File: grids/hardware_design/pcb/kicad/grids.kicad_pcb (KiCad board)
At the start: 2 copper layers, 78.1 x 102.9 mm, 108 parts, among them IC1 ATMEGA328P-AU, IC2 LM4040 5.0V, IC3 MCP6002, IC4 MCP6002, IC5 MCP6002, IC6 74HC595D, IC7 LM1117-5.0, J1 PJ301WQP, J10 PJ301WQP, J11 PJ301WQP, J12 PJ301WQP, J13 PJ301WQP, J14 PJ301WQP, J16 M05X2PTH, J2 PJ301WQP, J3 PJ301WQP, J4 PJ301WQP, J5 PJ301WQP, J6 PJ301WQP, J7 PJ301WQP, J8 PJ301WQP, J9 PJ301WQP, Q1 20MHz, Q2 MMBT3904, Q3 MMBT3904, SW1 LP4OA1PBCT

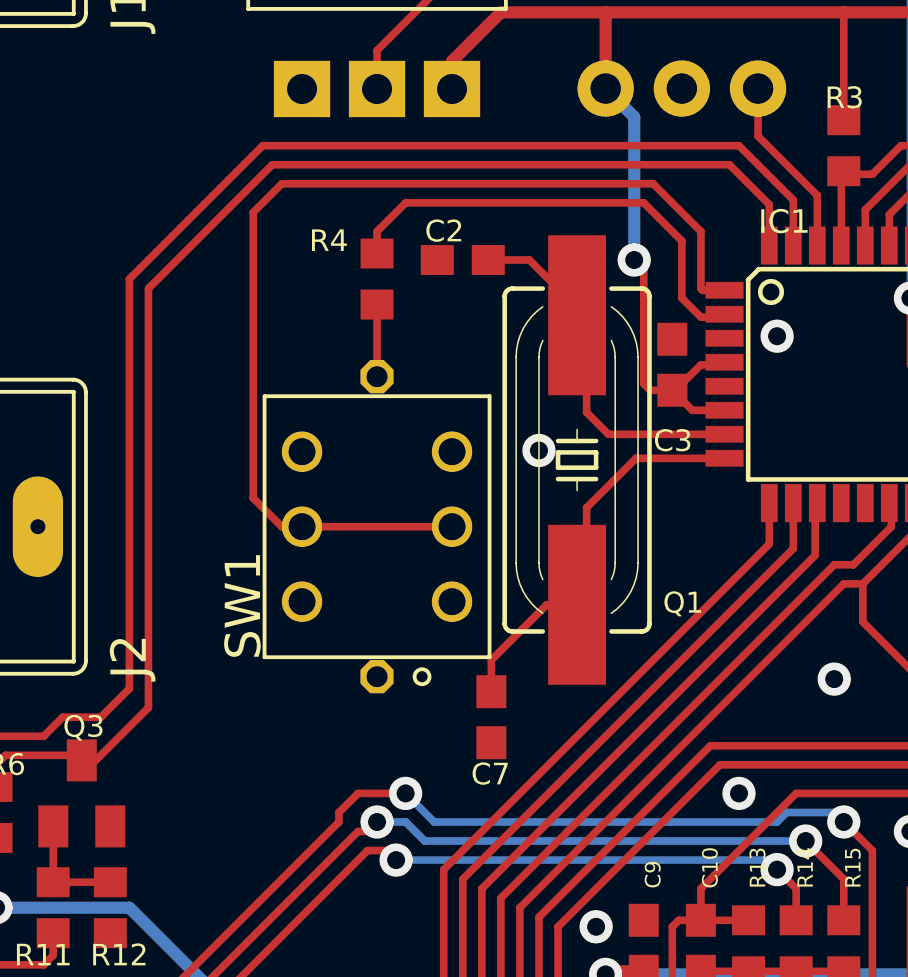
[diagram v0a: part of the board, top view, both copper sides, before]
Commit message: change LED/SW and crystal
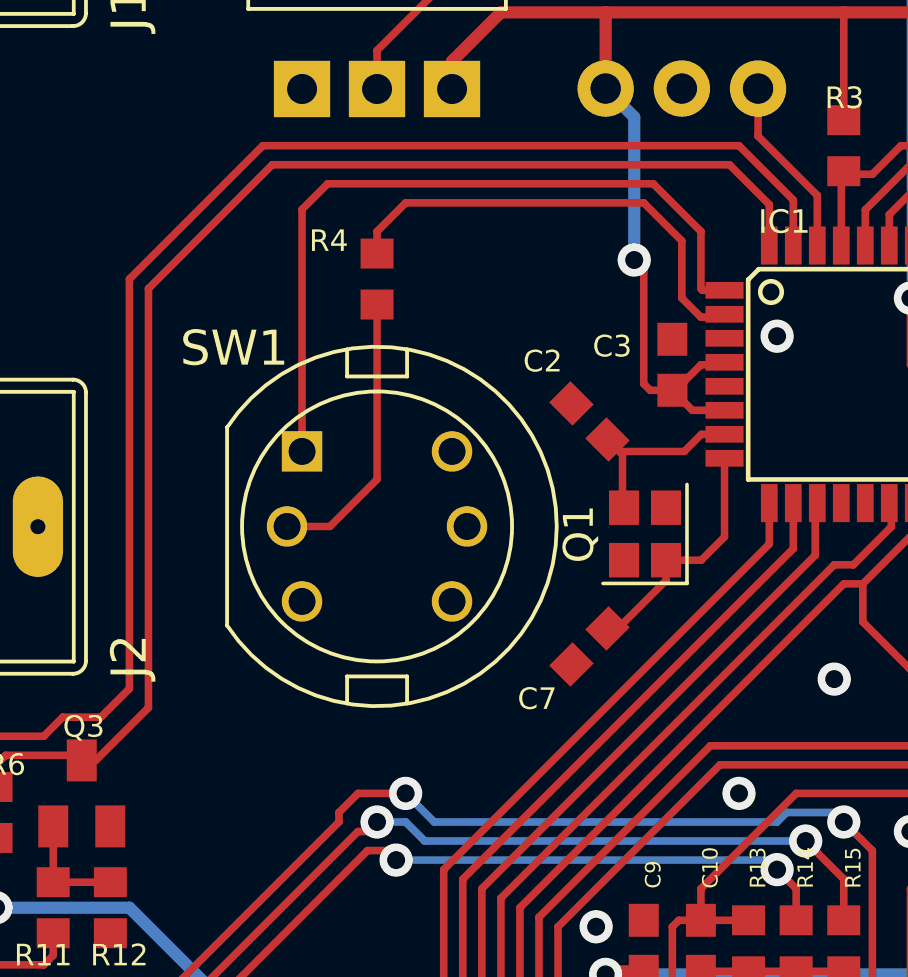
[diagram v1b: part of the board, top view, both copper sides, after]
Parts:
- removed U$1: , grids:EURORACK_TEMPLATE
- removed U$2: , grids:ROHS_BIG
- IC6: value 74HC595D -> 74595D
- J15: value (none) -> AVR_SPI_PRG_6PTH
- JP1, JP2: value (none) -> M03PTH
- L1: value (none) -> WE-CBF_0603
- LED2, LED3, LED4: value (none) -> LED3MM
- Q1: footprint grids:HC49UP -> Crystal:Crystal_SMD_2520-4Pin_2.5x2.0mm
- SW1: value LP4OA1PBCT -> SW_MEC_5G_2LED; footprint grids:LP4OA1PBCT -> Supercell 1.3:C&K_D6R
- moved C2 6.84 mm to (139.4, 78.0), turned to -45 degrees
- moved C7 4.03 mm to (139.4, 85.5), turned to 45 degrees
- moved Q1 3.35 mm to (141.2, 81.8)
- turned SW1 to 0 degrees
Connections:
- net AREF renamed /AREF
- net CH1_CV renamed /CH1_CV
- net CH2_CV renamed /CH2_CV
- net CH3_CV renamed /CH3_CV
- net CLOCK_OUT renamed Net-(IC6-Pad6)
- net GATE1_IN renamed Net-(J1-PadTIP)
- net GATE2_IN renamed Net-(J2-PadTIP)
- net GATE2_LED renamed Net-(LED4-PadA)
- net GATE3_LED renamed Net-(LED3-PadA)
- net GATE4_LED renamed Net-(LED2-PadA)
- net IN_CLOCK renamed /IN_CLOCK
- net IN_MIDI renamed /IN_MIDI
- net IN_RESET renamed /IN_RESET
- net LED_CH1 renamed /LED_CH1
- net LED_CH2 renamed /LED_CH2
- net LED_CH3 renamed /LED_CH3
- net LED_CLOCK renamed /LED_CLOCK
- net MISO renamed /MISO
- net MOSI renamed /MOSI
- net RANDOM_GATE renamed Net-(IC6-Pad7)
- net REF_-5 renamed /REF_-5
- net RESET renamed /RESET
- net RND_CV renamed /RND_CV
- net SCK renamed /SCK
- net SS renamed /SS
- net TEMPO renamed /TEMPO
- net X_CV renamed /X_CV
- net Y_CV renamed /Y_CV
- C2 pad 2: N$83 -> Net-(C2-Pad2)
- IC1 pad 1: SW_RESET -> /SW_RESET
- IC1 pad 12: (no net) -> unconnected-(IC1-Pad12)
- IC1 pad 13: (no net) -> unconnected-(IC1-Pad13)
- IC1 pad 22: (no net) -> unconnected-(IC1-Pad22)
- IC1 pad 7: N$83 -> Net-(C2-Pad2)
- IC6 pad 9: (no net) -> unconnected-(IC6-Pad9)
- J1 pad SW: (no net) -> unconnected-(J1-PadSW)
- J10 pad SW: (no net) -> unconnected-(J10-PadSW)
- J11 pad SW: (no net) -> unconnected-(J11-PadSW)
- J12 pad SW: (no net) -> unconnected-(J12-PadSW)
- J13 pad SW: (no net) -> unconnected-(J13-PadSW)
- J14 pad SW: (no net) -> unconnected-(J14-PadSW)
- J16 pad 2: (no net) -> unconnected-(J16-Pad2)
- J2 pad SW: (no net) -> unconnected-(J2-PadSW)
- J3 pad SW: (no net) -> unconnected-(J3-PadSW)
- J4 pad SW: (no net) -> unconnected-(J4-PadSW)
- J5 pad SW: (no net) -> unconnected-(J5-PadSW)
- J6 pad SW: (no net) -> unconnected-(J6-PadSW)
- J7 pad SW: (no net) -> unconnected-(J7-PadSW)
- J8 pad SW: (no net) -> unconnected-(J8-PadSW)
- J9 pad SW: (no net) -> unconnected-(J9-PadSW)
- Q1 pad 2: N$83 -> unconnected-(Q1-Pad2)
- R4 pad 2: GATE1_LED -> Net-(SW1-Pad2)
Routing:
- net SW_RESET: track 35.2 -> 0.00 mm
- net /SW_RESET: track 0.00 -> 25.1 mm
- net N$83: track 12.1 -> 0.00 mm
- net Net-(SW1-Pad2): track 0.00 -> 9.48 mm
- net Net-(C2-Pad2): track 0.00 -> 6.80 mm
- net Net-(C7-Pad2): track 13.3 -> 8.18 mm
- net GATE1_LED: track 2.41 -> 0.00 mm
- net GND: vias 65 -> 64

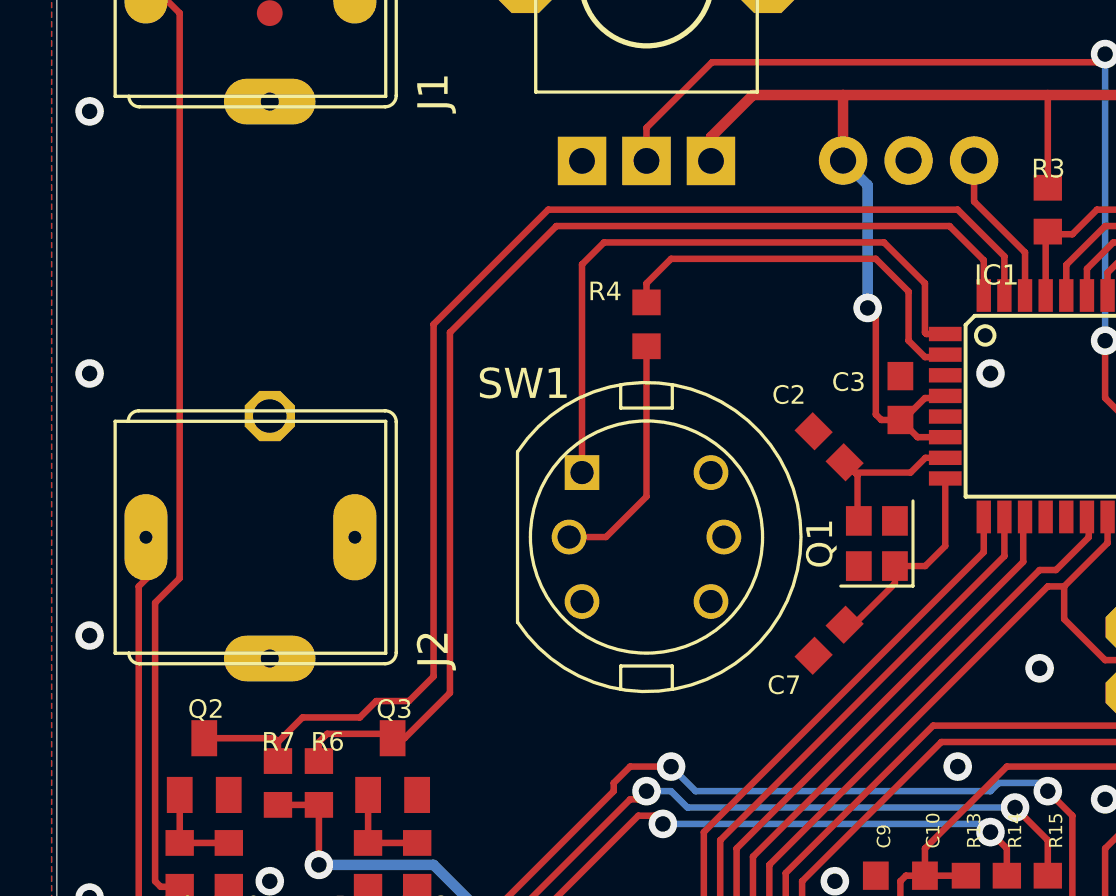
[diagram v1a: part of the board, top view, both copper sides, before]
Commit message: add horizontal smd programming header (traces not drawn yet)
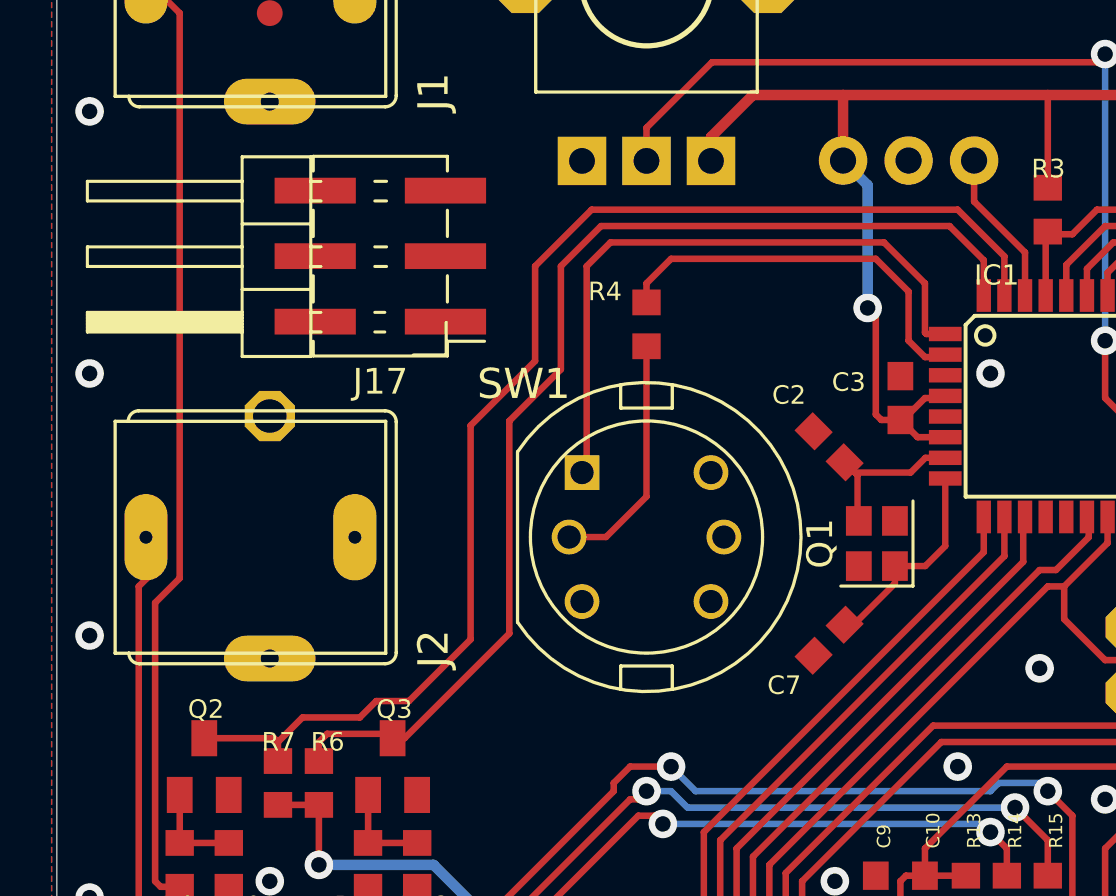
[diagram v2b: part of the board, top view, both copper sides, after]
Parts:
- added J17: AVR_SPI_PRG_6PTH, Connector_PinHeader_2.54mm:PinHeader_2x03_P2.54mm_Horizontal_SMD, F.Cu at (122.0, 70.6)
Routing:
- net /IN_RESET: track 45.0 -> 44.0 mm
- net /IN_CLOCK: track 50.6 -> 49.6 mm

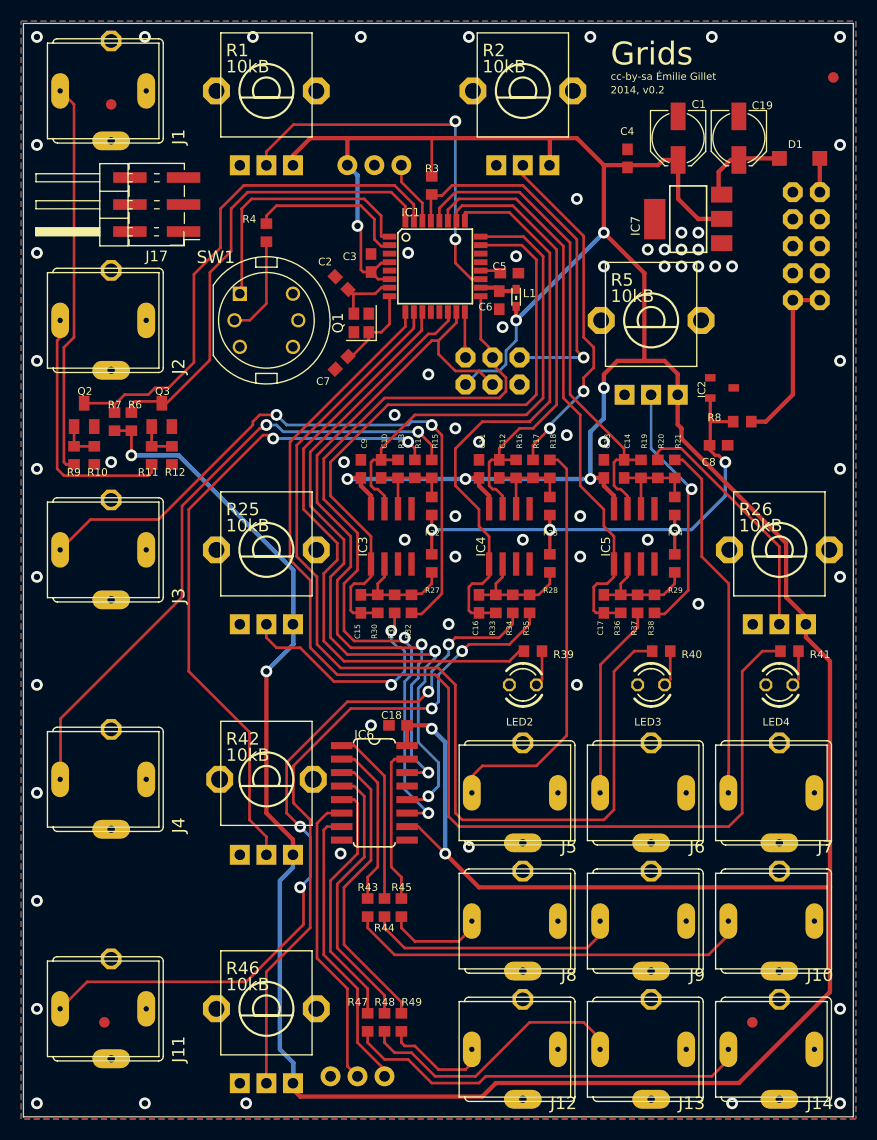
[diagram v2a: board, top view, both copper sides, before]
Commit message: changed jacks
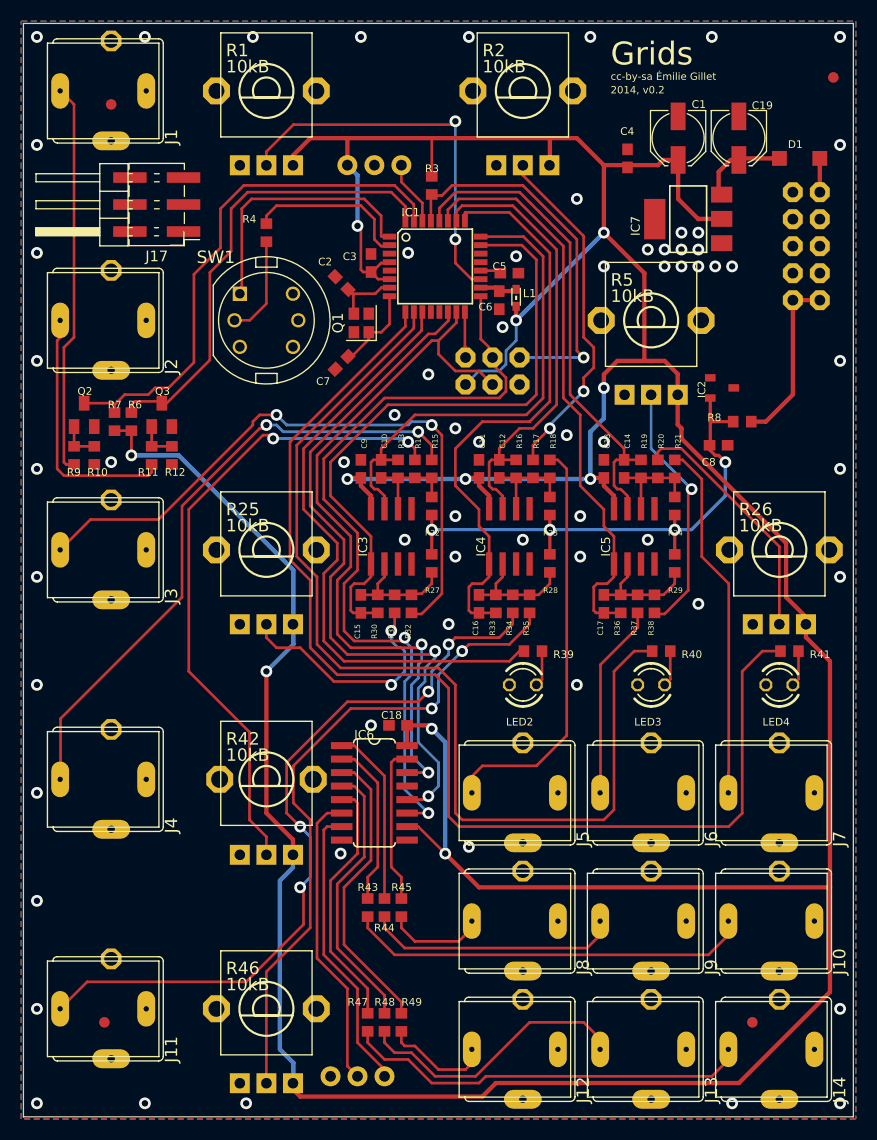
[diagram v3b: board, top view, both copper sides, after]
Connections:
- J1 pad GND2: GND -> (no net)
- J10 pad GND2: GND -> (no net)
- J11 pad GND2: GND -> (no net)
- J12 pad GND2: GND -> (no net)
- J13 pad GND2: GND -> (no net)
- J14 pad GND2: GND -> (no net)
- J2 pad GND2: GND -> (no net)
- J3 pad GND2: GND -> (no net)
- J4 pad GND2: GND -> (no net)
- J5 pad GND2: GND -> (no net)
- J6 pad GND2: GND -> (no net)
- J7 pad GND2: GND -> (no net)
- J8 pad GND2: GND -> (no net)
- J9 pad GND2: GND -> (no net)

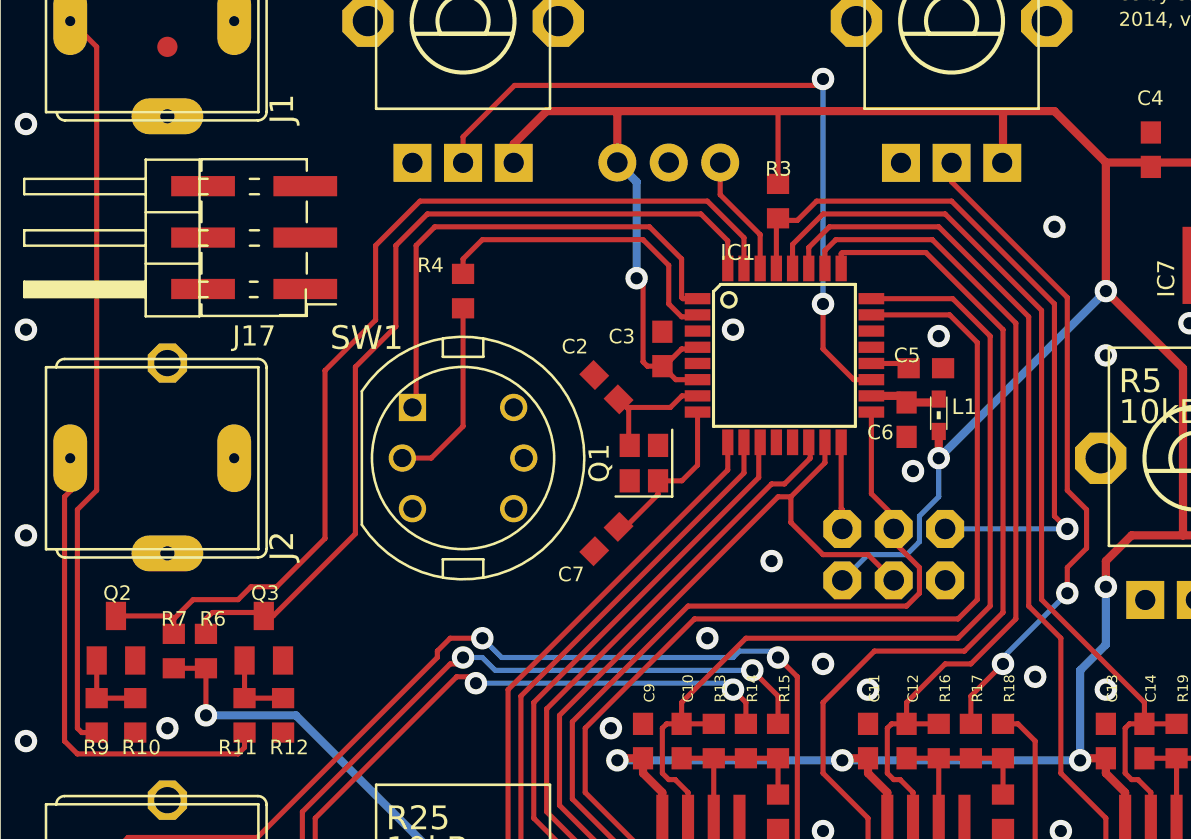
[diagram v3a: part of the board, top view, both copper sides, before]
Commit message: draw pcb traces for new header
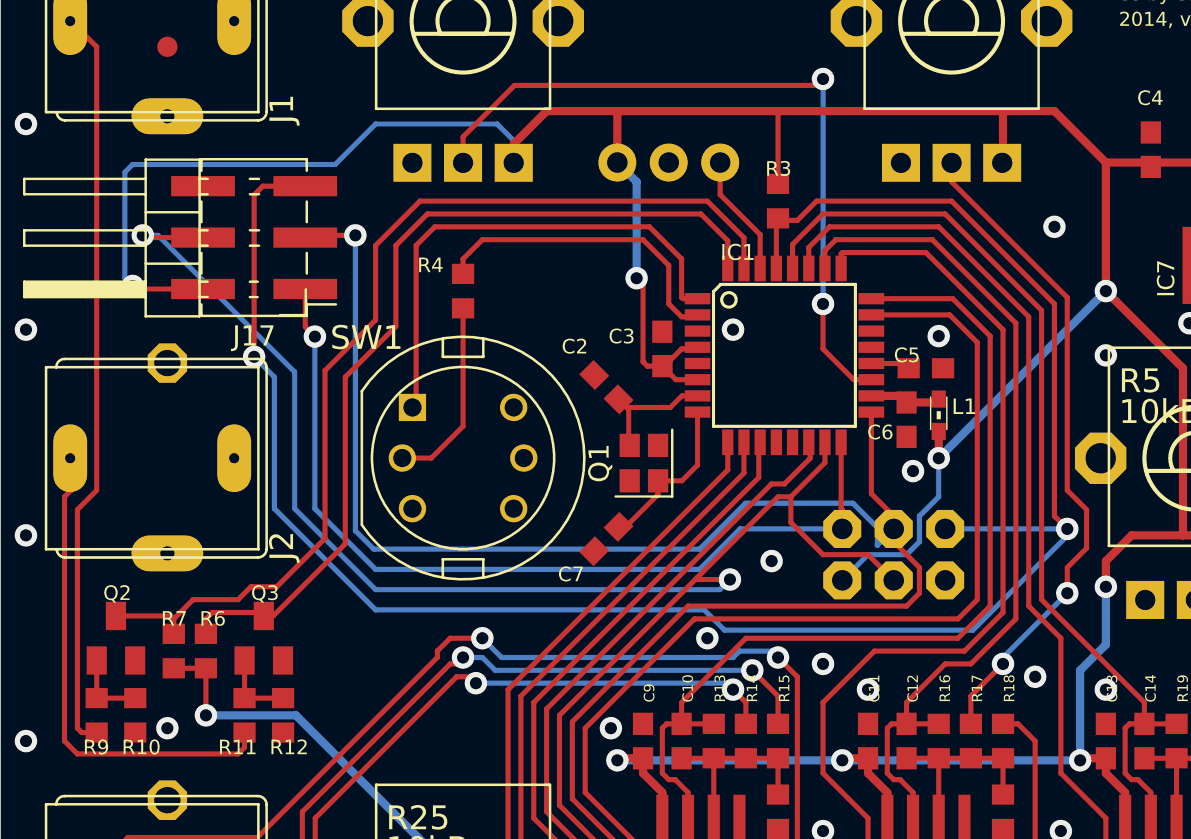
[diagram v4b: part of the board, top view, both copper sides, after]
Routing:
- net /RESET: track 36.1 -> 98.7 mm, vias 1 -> 2
- net /SCK: track 73.9 -> 120.7 mm, vias 2 -> 3
- net /MOSI: track 69.2 -> 114.5 mm, vias 2 -> 4
- net /MISO: track 4.30 -> 43.5 mm, vias 0 -> 1
- net +5V: track 423.2 -> 454.1 mm, vias 11 -> 12
